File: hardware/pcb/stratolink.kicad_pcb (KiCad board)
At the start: 2 copper layers, 23.4 x 57.3 mm, 46 parts, among them J1 Conn_Header_JST_PH_1x02_P2mm_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, J2 Conn_Header_JST_PH_1x02_P2mm_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, J20 Conn_ARM_SWD_TagConnect_TC203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, J3 Conn_PinHeader_1x07_P2.54mm_V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, J4 Conn_PinHeader_1x07_P2.54mm_V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, U2 RAK3172

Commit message: mounting holes for solar ++ final gerber v1
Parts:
- moved J3 1.13 mm to (54.4, 69.2)
- moved J4 1.11 mm to (75.5, 69.2)
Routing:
- net GND: track 140.8 -> 187.1 mm, vias 83 -> 84
- net TX: track 49.5 -> 45.8 mm
- net PA10: track 7.44 -> 9.62 mm
- net +3.3V: track 116.1 -> 114.6 mm
- net RX: track 42.0 -> 40.5 mm
- net PA15: track 10.8 -> 9.52 mm
- net VSTOR: track 59.3 -> 60.4 mm
- net PB5: track 58.7 -> 57.6 mm
- net BOOT0: track 24.1 -> 23.0 mm
- net RSTN: track 60.7 -> 59.7 mm
- net PA1: track 31.6 -> 30.6 mm
- net PA9: track 19.5 -> 20.3 mm, vias 2 -> 1
- net PA8: track 19.4 -> 18.7 mm
- net PB2: track 7.47 -> 6.80 mm
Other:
- outline, holes or cut-outs redrawn

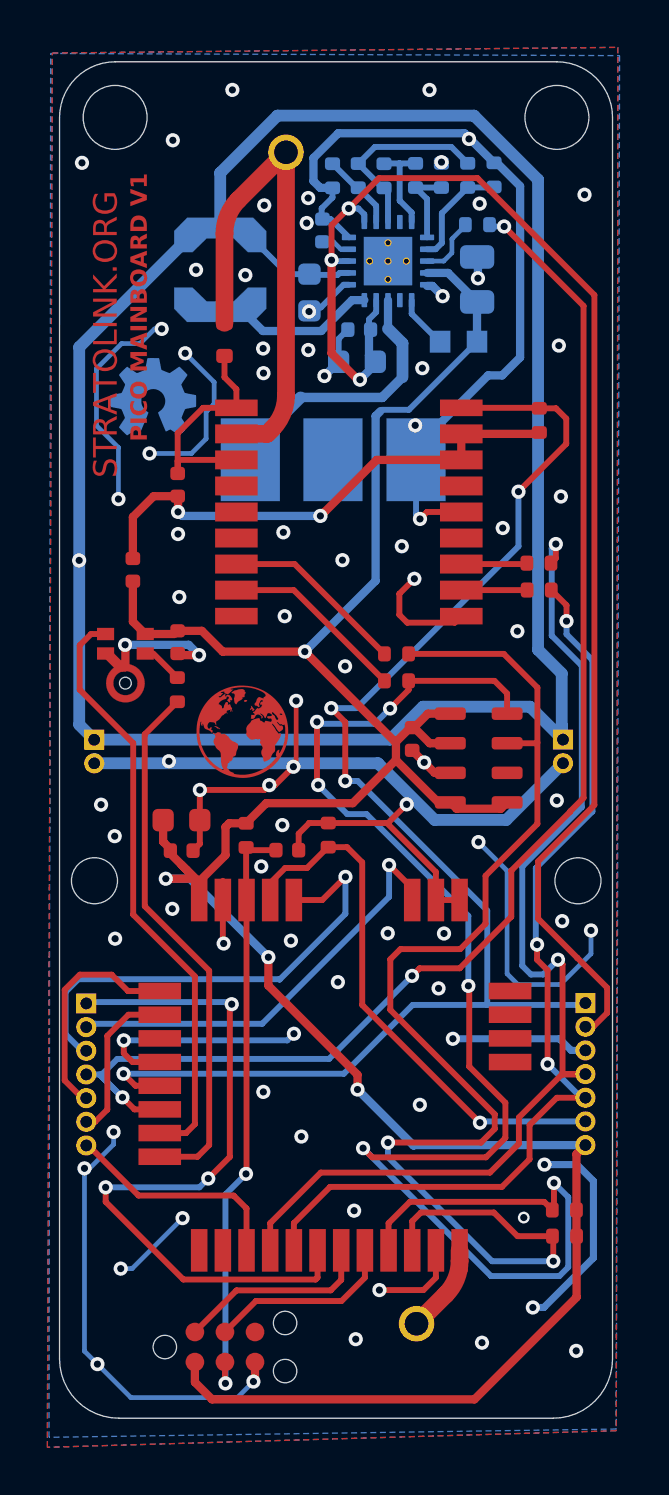
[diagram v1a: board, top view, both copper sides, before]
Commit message: accelerometer + spectral + temp init
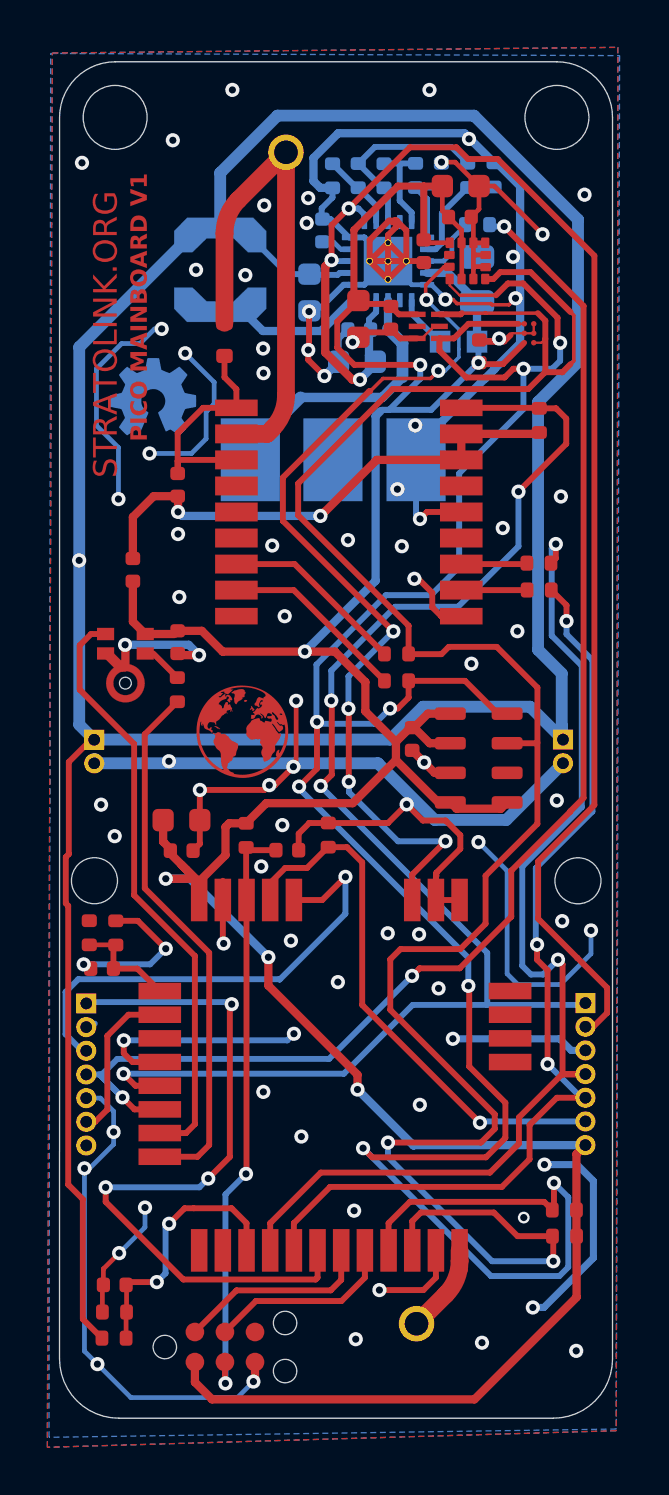
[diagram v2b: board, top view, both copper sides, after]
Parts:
- added C12: 100nF, Capacitor_SMD:C_0402_1005Metric, F.Cu at (71.0, 41.6)
- added C14: 100nF, Capacitor_SMD:C_0402_1005Metric, F.Cu at (67.3, 40.2)
- added C15: 100nF, Capacitor_SMD:C_0402_1005Metric, F.Cu at (55.6, 81.1)
- added C16: 4.7μF, Capacitor_SMD:C_0603_1608Metric, F.Cu at (65.9, 40.3)
- added C17: 100nF, Capacitor_SMD:C_0402_1005Metric, F.Cu at (55.1, 67.7)
- added C19: 100nF, Capacitor_SMD:C_0402_1005Metric, F.Cu at (70.2, 36.0)
- added C20: 100nF, Capacitor_SMD:C_0402_1005Metric, F.Cu at (68.7, 37.4)
- added C21: 10μF, Capacitor_SMD:C_0603_1608Metric, F.Cu at (70.3, 34.6)
- added R19: 1MΩ, Resistor_SMD:R_0402_1005Metric, F.Cu at (55.6, 83.3)
- added R21: 1MΩ, Resistor_SMD:R_0402_1005Metric, F.Cu at (55.6, 82.2)
- added R22: 1MΩ, Resistor_SMD:R_0402_1005Metric, F.Cu at (54.6, 66.2)
- added R23: 1MΩ, Resistor_SMD:R_0402_1005Metric, F.Cu at (55.7, 66.2)
- added U5: TMP117NAIYBGR, lib:BGA6N40P3X2_148X95X53, F.Cu at (73.1, 40.9)
- added U6: ~, lib:21-0147E, F.Cu at (68.9, 40.6)
- added U7: LIS2DH12TR, lib:PQFN50P200X200100-12N, F.Cu at (70.5, 37.8)
- C4: value 0.1µF -> 100nF
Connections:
- J3 pad 2: PA8 -> GND
- J3 pad 5: PA10 -> GND
- J3 pad 7: PA15 -> GND
- U1 pad 21: unconnected-(U1-EP-Pad21) -> GND
- U1 pad 22: (no net) -> GND
- U1 pad 23: (no net) -> GND
- U1 pad 24: (no net) -> GND
- U1 pad 25: (no net) -> GND
- U1 pad 26: (no net) -> GND
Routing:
- net GND: track 187.1 -> 244.5 mm, vias 84 -> 86
- net SCL: track 62.6 -> 100.0 mm, vias 6 -> 8
- net SDA: track 54.8 -> 91.9 mm
- net +3.3V: track 114.6 -> 145.2 mm, vias 4 -> 6
- net +SOLAR: track 94.8 -> 122.7 mm
- net PA8: track 18.7 -> 38.3 mm, vias 1 -> 6
- net PA10: track 9.62 -> 4.50 mm
- net VSTOR: track 60.4 -> 62.8 mm
- net PA15: track 9.52 -> 11.2 mm, vias 0 -> 2
- net RSTN: track 59.7 -> 60.7 mm

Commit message: [PROD] Stratolink Pico Mainboard V1
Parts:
- added D1: ESD9B3.3ST5G, Diode_SMD:D_SOD-523, F.Cu at (71.1, 82.8)
- moved D3 3.73 mm to (60.3, 37.4)
- moved C16 0.13 mm to (66.1, 40.3)
- renumbered R17 to FB1
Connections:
- J3 pad 4: PB5 -> GND
- J4 pad 1: RSTN -> GND
- U1 pad 17: unconnected-(U1-NC-Pad17) -> GND
- U1 pad 9: unconnected-(U1-NC-Pad9) -> GND
- U3 pad 6: unconnected-(U3-V_BCKP-Pad6) -> Net-(U3-VCC)
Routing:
- net VSTOR: track 62.8 -> 98.3 mm, vias 3 -> 6
- net GND: track 244.5 -> 269.5 mm, vias 86 -> 87
- net RSTN: track 60.7 -> 56.2 mm
- net Net-(AE2-A): track 21.6 -> 17.8 mm
- net +3.3V: track 145.2 -> 142.0 mm
- net PB5: track 57.6 -> 55.4 mm
- net Net-(AE1-A): track 3.80 -> 5.84 mm
- net Net-(U3-VCC): track 22.1 -> 23.2 mm
- net +SOLAR: track 122.7 -> 123.8 mm, vias 1 -> 0

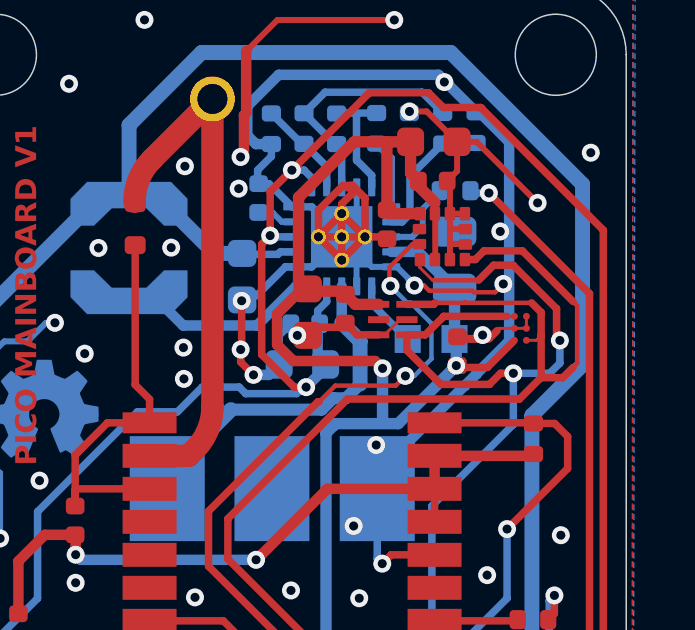
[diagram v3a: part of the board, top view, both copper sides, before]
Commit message: [FIX] updated spectralsensor footprint GERBER
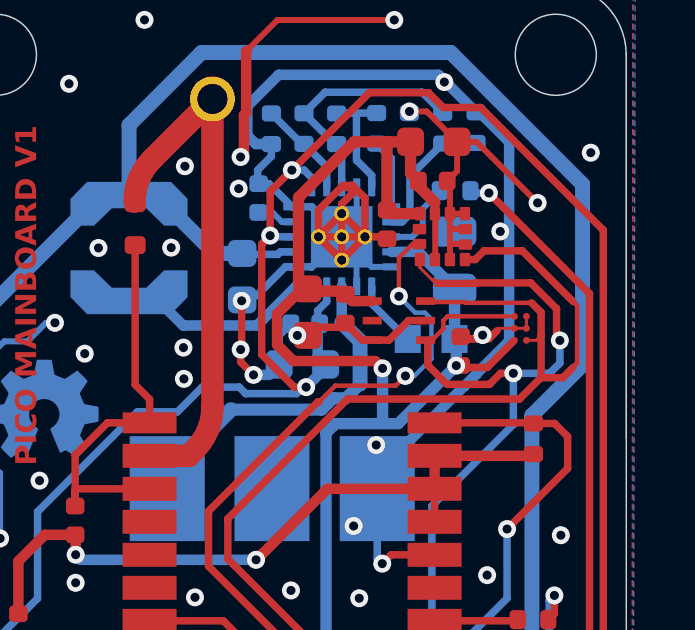
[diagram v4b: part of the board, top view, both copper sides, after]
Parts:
- U6: footprint lib:21-0147E -> lib:SMD6_LTR-390UV-01_LTO-L
- moved U6 0.21 mm to (69.1, 40.6)
- moved C12 0.11 mm to (71.2, 41.6)
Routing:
- net GND: track 269.5 -> 266.0 mm, vias 87 -> 85
- net SCL: track 100.0 -> 98.6 mm
- net SDA: track 91.9 -> 91.3 mm
